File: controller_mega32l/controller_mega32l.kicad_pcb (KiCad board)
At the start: 2 copper layers, 262.9 x 144.8 mm, 81 parts, among them IC1 ATMEGA32-A, IC2 MAX481CPA, J1 RJ45, K1 CONN_PWR_OUT, P1 CONN_PWR_IN, P2 CONN_PWM_OUT, P3 CONN_3X2, P4 CONN_JTAG, P5 CONN_ADC, P6 CONN_GPIO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

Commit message: PCB signal layer
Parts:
- IC1: footprint TQFP44 -> Package_QFP:TQFP-44_10x10mm_P0.8mm
- IC2, J1, K1, P2, P3, P4, P5, P6, Q1, R14, R4: moved to F.Cu
- R17, R19, R20, R23, R25, R29, R30, R32: footprint C1 -> Resistor_THT:R_Axial_DIN0309_L9.0mm_D3.2mm_P15.24mm_Horizontal
- R27: moved to B.Cu
- R3: footprint C1 -> Resistor_THT:R_Axial_DIN0309_L9.0mm_D3.2mm_P20.32mm_Horizontal; moved to F.Cu
- moved R28 83.4 mm to (140.7, 83.8), turned to 270 degrees
- moved R18 52.9 mm to (118.6, 112.0)
- moved R3 26.5 mm to (182.6, 73.7), turned to 270 degrees
- moved R32 24.9 mm to (186.9, 103.4), turned to 180 degrees
- moved R27 20.8 mm to (83.8, 99.6)
- moved R29 20.1 mm to (187.5, 140.5)
- moved K1 19.4 mm to (107.4, 68.6), turned to 270 degrees
- moved P2 16.9 mm to (126.0, 69.6)
- moved R30 16.5 mm to (178.8, 140.5)
- moved D25 16.5 mm to (140.0, 123.2)
- moved R23 13.3 mm to (169.7, 140.2)
- moved R25 12.7 mm to (151.9, 139.7)
- moved R14 12.1 mm to (108.0, 86.4)
- moved P4 12.1 mm to (171.2, 73.4), turned to 270 degrees
- moved D14 10.2 mm to (156.4, 102.5)
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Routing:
- net (no net): track 156.0 -> 0.00 mm, vias 5 -> 0
- net DGND: track 0.00 -> 94.1 mm, vias 0 -> 3
- net +5VD: track 0.00 -> 77.9 mm
- net Net-(D14-Pad3): track 0.00 -> 49.6 mm, vias 0 -> 4
- net Net-(C2-Pad1): track 0.00 -> 43.1 mm
- net /TMS: track 0.00 -> 42.0 mm
- net /TDI: track 0.00 -> 37.5 mm
- net Net-(C4-Pad1): track 0.00 -> 36.4 mm
- net Net-(IC1-Pad12): track 0.00 -> 33.9 mm
- net Net-(IC1-Pad13): track 0.00 -> 27.6 mm
- net Net-(D8-Pad2): track 0.00 -> 20.5 mm
- net Net-(D10-Pad2): track 0.00 -> 20.1 mm
- net Net-(IC1-Pad26): track 0.00 -> 19.6 mm
- net /TDO: track 0.00 -> 19.5 mm
- net Net-(D11-Pad2): track 0.00 -> 15.9 mm
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- added copper zone on B.Cu, net +5VD
- removed copper zone on F.Cu, net +5VD
- removed copper zone on B.Cu, net DGND
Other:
- net class Default: clearance 0.35 -> 0.25; via_dia 1.27 -> 2.54
- rule trace_clearance: 0.35 -> 0.25

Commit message: PCB changes
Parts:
- removed D29: D_Schottky_x2_KCom_AAK, TO_SOT_Packages_SMD:SOT-23_Handsoldering
- D12: footprint TO_SOT_Packages_SMD:SOT-23_Handsoldering -> digikey-footprints:SOT-23-3
- P1: moved to F.Cu
- R1, R13, R27, R34: footprint C1 -> Resistor_THT:R_Axial_DIN0411_L9.9mm_D3.6mm_P15.24mm_Horizontal; moved to F.Cu
- R17, R19, R20, R23, R25, R29, R30, R32: footprint Resistor_THT:R_Axial_DIN0309_L9.0mm_D3.2mm_P15.24mm_Horizontal -> Resistor_THT:R_Axial_DIN0411_L9.9mm_D3.6mm_P15.24mm_Horizontal; moved to F.Cu
- R26, R4: footprint C1 -> Resistor_THT:R_Axial_DIN0411_L9.9mm_D3.6mm_P15.24mm_Horizontal
- R3: footprint Resistor_THT:R_Axial_DIN0309_L9.0mm_D3.2mm_P20.32mm_Horizontal -> Resistor_THT:R_Axial_DIN0411_L9.9mm_D3.6mm_P20.32mm_Horizontal
- moved R26 18.1 mm to (76.7, 93.7)
- moved R25 17.8 mm to (169.7, 140.2)
- moved R1 16.9 mm to (61.0, 53.6)
- moved R4 15.5 mm to (178.1, 97.5)
- moved R13 13.7 mm to (87.4, 108.2)
- moved R20 9.40 mm to (151.4, 140.0)
- moved R23 9.40 mm to (160.3, 140.5)
- moved R19 6.37 mm to (142.7, 145.3)
- moved P1 6.10 mm to (45.7, 63.8)
- moved R17 5.73 mm to (135.9, 145.3)
- moved R27 4.79 mm to (86.4, 103.6)
- moved R34 4.75 mm to (48.5, 89.2)
- moved D18 3.23 mm to (65.5, 98.8)
- moved K1 0.80 mm to (107.7, 69.3)
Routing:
- net DGND: track 94.1 -> 84.7 mm

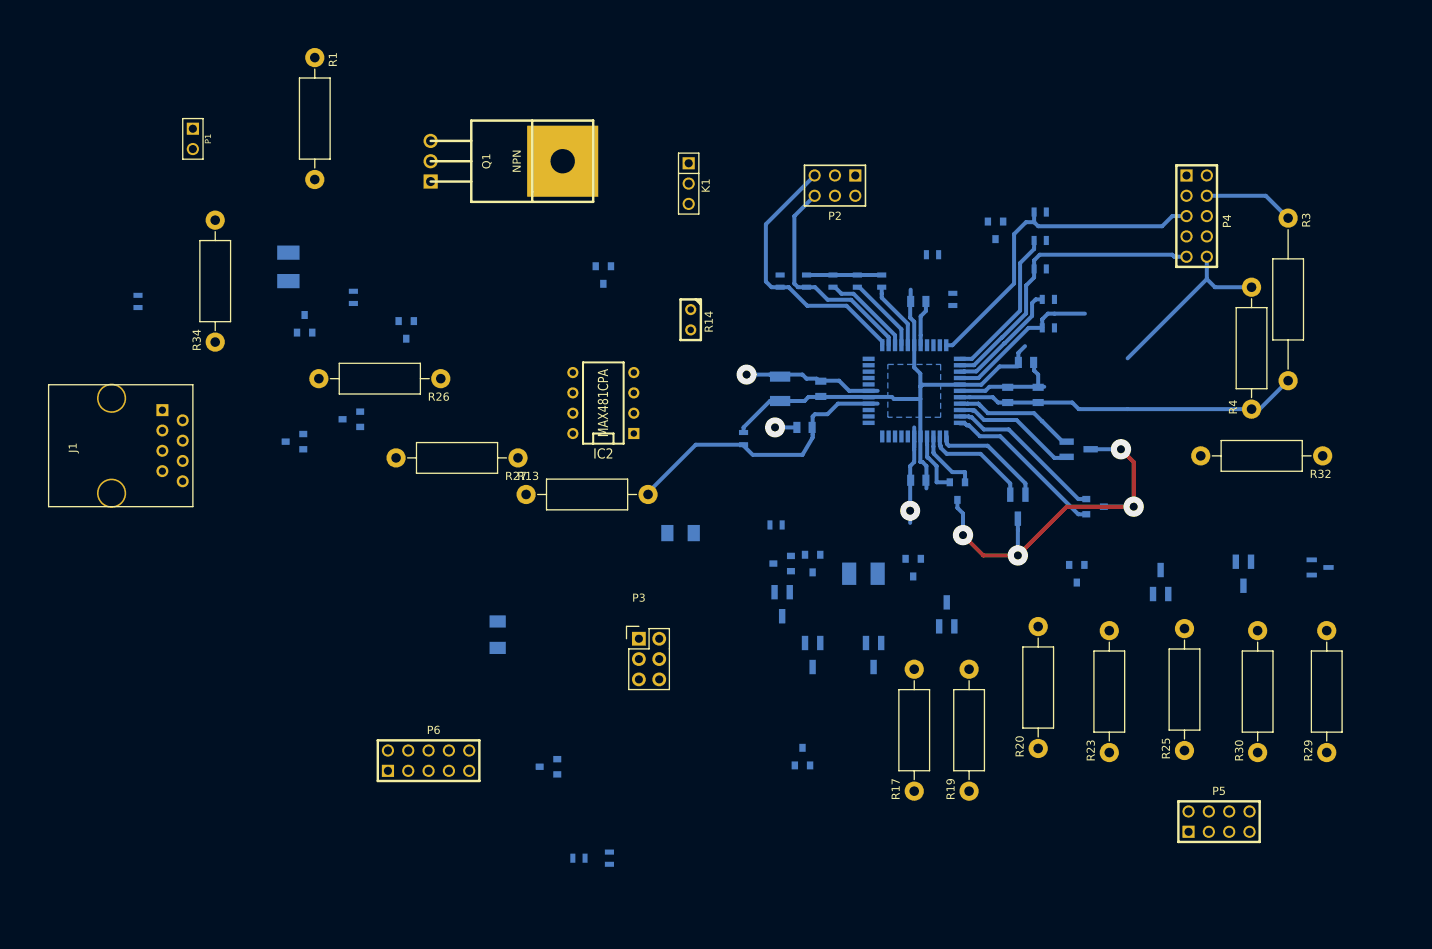
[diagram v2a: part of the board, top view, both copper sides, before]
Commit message: New PCB routes, footprints updated, KiCAD up version to 5.1
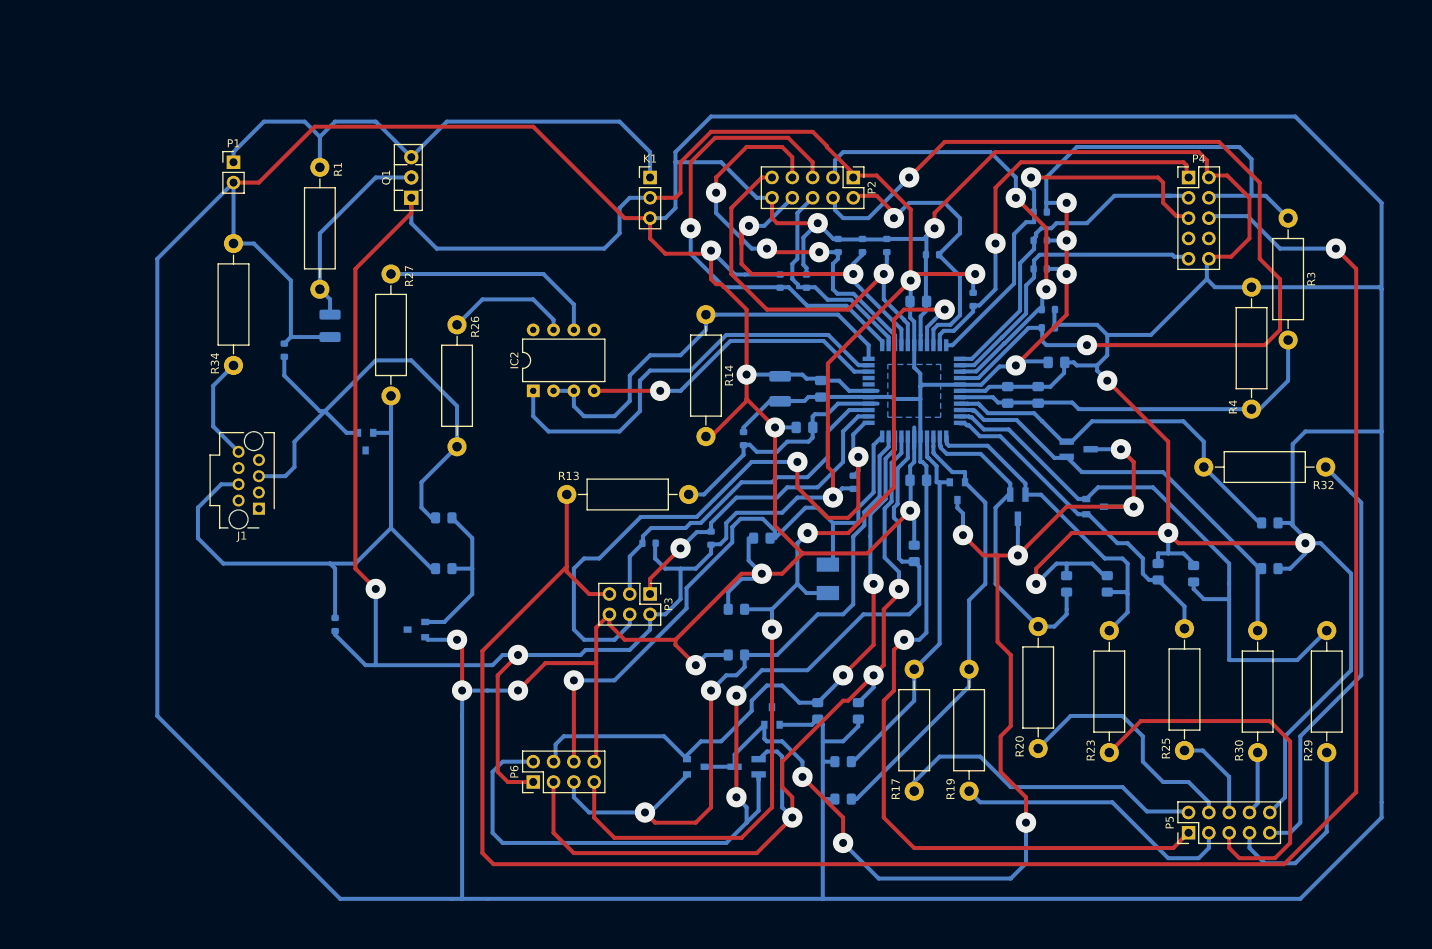
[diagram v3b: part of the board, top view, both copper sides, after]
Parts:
- C1: footprint SM1210 -> Capacitor_SMD:C_1210_3225Metric_Pad1.33x2.70mm_HandSolder
- C2, C3, C4, C5, C6, C7, C8: footprint SM0805 -> Capacitor_SMD:C_0805_2012Metric_Pad1.18x1.45mm_HandSolder
- D1: footprint SM1210L -> Diode_SMD:D_1210_3225Metric
- D10, D2, D25, D4, D8: footprint TO_SOT_Packages_SMD:SOT-23_Handsoldering -> Diode_SMD:D_0805_2012Metric_Pad1.15x1.40mm_HandSolder
- D11, D13, D18, D23, D26, D28, D5, D7: footprint SOT23 -> Diode_SMD:D_0805_2012Metric_Pad1.15x1.40mm_HandSolder
- D12: footprint digikey-footprints:SOT-23-3 -> Diode_SMD:D_0805_2012Metric_Pad1.15x1.40mm_HandSolder
- D21, D22: footprint SM1206 -> Diode_SMD:D_0805_2012Metric_Pad1.15x1.40mm_HandSolder
- IC2: footprint DIP-8__300 -> Package_DIP:DIP-8_W7.62mm
- J1: footprint RJ45_8 -> Connector_RJ:RJ45_Plug_Metz_AJP92A8813
- K1: footprint PIN_ARRAY_3X1 -> Connector_PinHeader_2.54mm:PinHeader_1x03_P2.54mm_Vertical
- P1: footprint PIN_ARRAY_2X1 -> Connector_PinHeader_2.54mm:PinHeader_1x02_P2.54mm_Vertical
- P2: footprint pin_array_3x2 -> Connector_PinHeader_2.54mm:PinHeader_2x05_P2.54mm_Vertical
- P3: footprint Pin_Headers:Pin_Header_Straight_2x03 -> Connector_PinHeader_2.54mm:PinHeader_2x03_P2.54mm_Vertical
- P4: footprint PIN_ARRAY_5x2 -> Connector_PinHeader_2.54mm:PinHeader_2x05_P2.54mm_Vertical
- P5: footprint pin_array_4x2 -> Connector_PinHeader_2.54mm:PinHeader_2x05_P2.54mm_Vertical
- P6: footprint PIN_ARRAY_5x2 -> Connector_PinHeader_2.54mm:PinHeader_2x04_P2.54mm_Vertical
- Q1: footprint TO220 -> Package_TO_SOT_THT:TO-126-3_Vertical
- R10, R11, R12, R15, R16, R18, R2, R21, R22, R24, R28, R31, R33, R5, R6, R7, R8, R9: footprint SM0603 -> Resistor_SMD:R_0603_1608Metric
- R14: footprint C1 -> Resistor_THT:R_Axial_DIN0411_L9.9mm_D3.6mm_P15.24mm_Horizontal
- R3: footprint Resistor_THT:R_Axial_DIN0411_L9.9mm_D3.6mm_P20.32mm_Horizontal -> Resistor_THT:R_Axial_DIN0411_L9.9mm_D3.6mm_P15.24mm_Horizontal
- moved D26 62.5 mm to (128.9, 135.3), turned to 90 degrees
- moved D23 50.3 mm to (113.7, 128.3)
- moved R31 47.3 mm to (63.5, 124.5), turned to 90 degrees
- moved R16 43.3 mm to (110.5, 113.7), turned to 90 degrees
- moved D7 40.7 mm to (160.0, 119.4)
- moved R15 39.7 mm to (102.7, 114.3), turned to 180 degrees
- moved D17 37.5 mm to (73.7, 125.1), turned to 270 degrees
- moved D5 31.9 mm to (154.9, 119.4), turned to 270 degrees
- moved D21 30.0 mm to (113.7, 122.6), turned to 0 degrees
- moved D13 29.8 mm to (77.1, 111.1)
- moved R27 27.9 mm to (70.5, 80.6), turned to 270 degrees
- moved D11 24.1 mm to (180.3, 117.5), turned to 180 degrees
- moved D18 22.0 mm to (77.1, 117.5), turned to 180 degrees
- moved D27 20.8 mm to (114.9, 142.2), turned to 270 degrees
- moved D25 20.1 mm to (123.8, 135.3), turned to 90 degrees
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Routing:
- net DGND: track 84.7 -> 1144.8 mm, vias 3 -> 15
- net +5VD: track 77.9 -> 535.7 mm, vias 0 -> 10
- net /-RESET: track 0.00 -> 256.7 mm, vias 0 -> 1
- net /GPIO_1: track 0.00 -> 121.8 mm, vias 0 -> 2
- net /GPIO_6: track 0.00 -> 119.5 mm, vias 0 -> 3
- net /GPIO_2: track 0.00 -> 112.1 mm, vias 0 -> 3
- net Net-(IC1-Pad26): track 19.6 -> 126.1 mm, vias 0 -> 2
- net Net-(D14-Pad3): track 49.6 -> 146.6 mm, vias 4 -> 7
- net /GPIO_4: track 0.00 -> 89.0 mm, vias 0 -> 2
- net /GPIO_3: track 0.00 -> 79.9 mm, vias 0 -> 2
- net /GPIO_5: track 0.00 -> 78.2 mm, vias 0 -> 1
- net Net-(IC1-Pad1): track 0.00 -> 78.2 mm, vias 0 -> 2
- net Net-(D15-Pad2): track 0.00 -> 70.9 mm
- net +24V: track 0.00 -> 68.7 mm
- net Net-(D13-Pad2): track 0.00 -> 66.3 mm
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
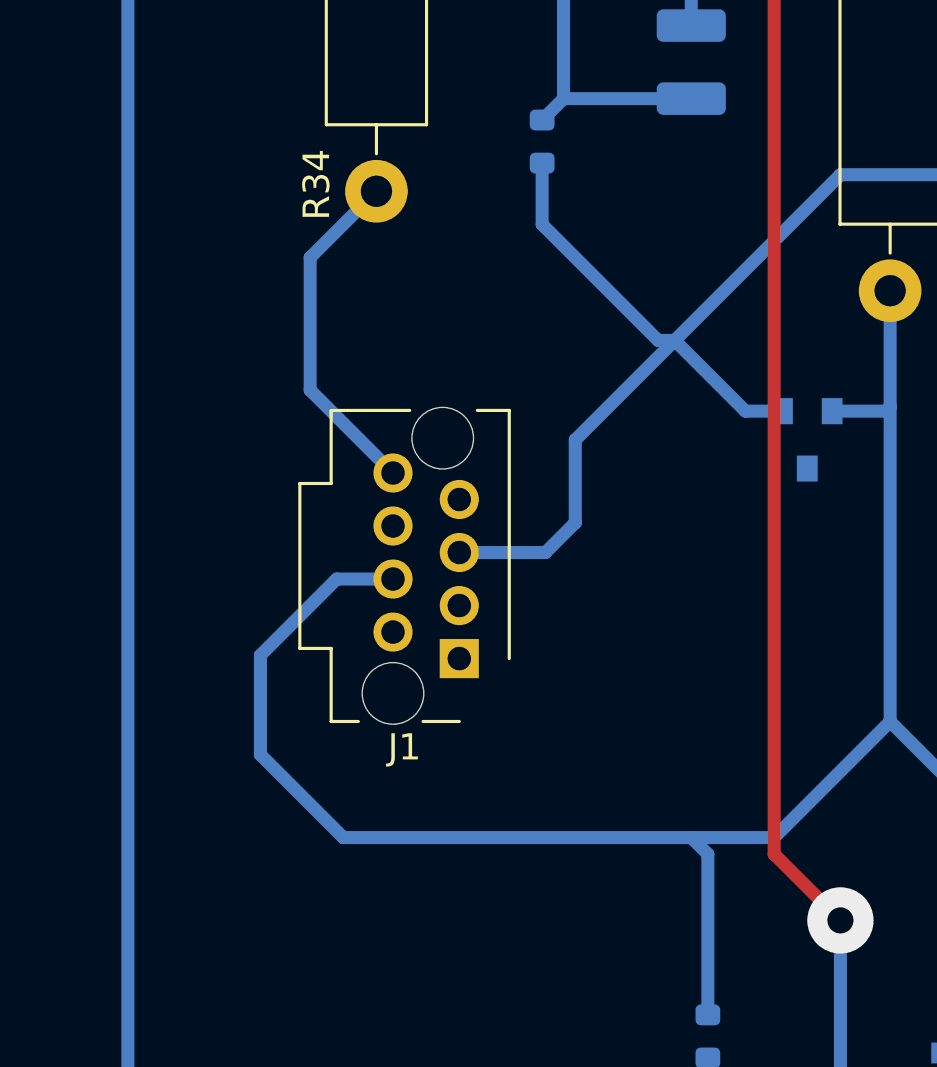
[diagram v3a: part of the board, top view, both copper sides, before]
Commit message: RJ-45 footprint updated, PCB screenshot added to docs
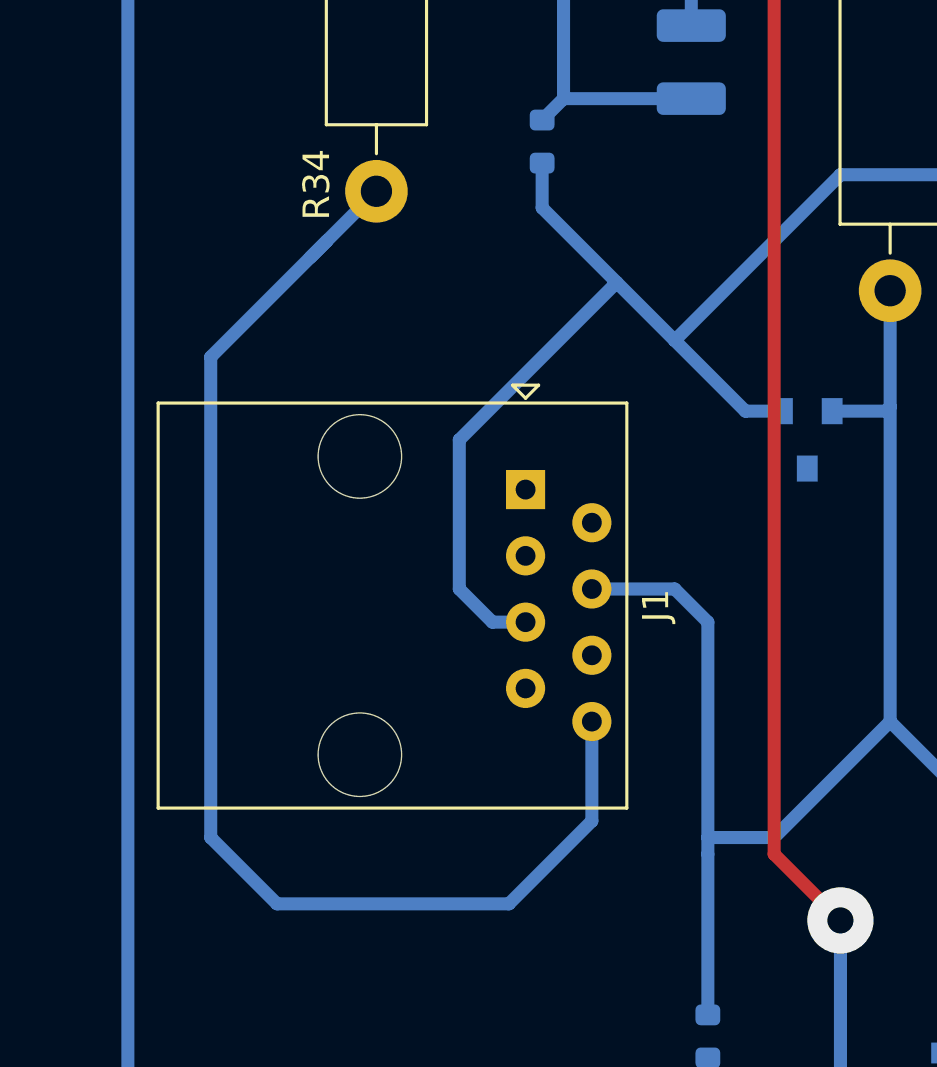
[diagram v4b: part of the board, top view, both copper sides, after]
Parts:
- J1: footprint Connector_RJ:RJ45_Plug_Metz_AJP92A8813 -> Connector_RJ:RJ45_Amphenol_54602-x08_Horizontal
- moved J1 6.96 mm to (56.5, 103.5), turned to 270 degrees
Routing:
- net Net-(J1-Pad8): track 13.2 -> 49.1 mm
- net Net-(D15-Pad2): track 70.9 -> 55.3 mm
- net Net-(D13-Pad2): track 66.3 -> 69.8 mm

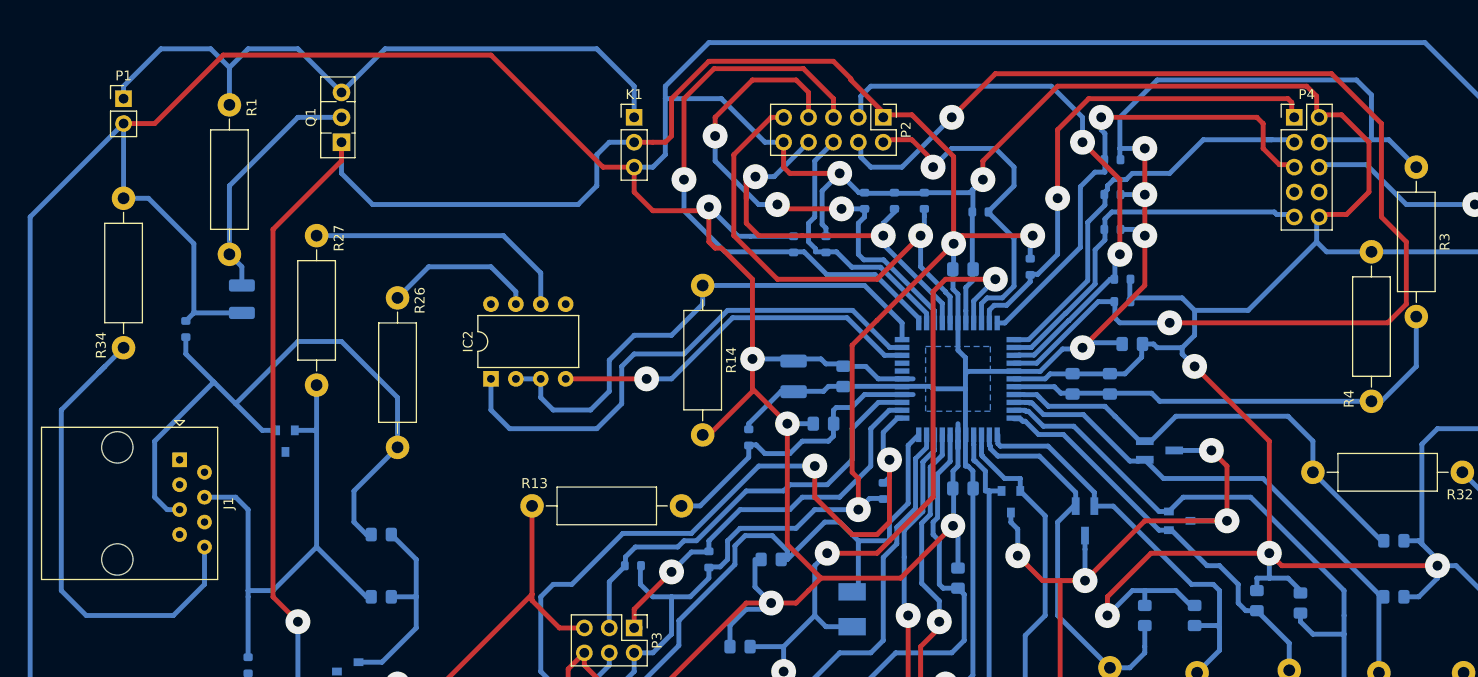
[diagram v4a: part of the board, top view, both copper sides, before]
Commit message: RJ-45 ground connections fixed, PCB texts placed right
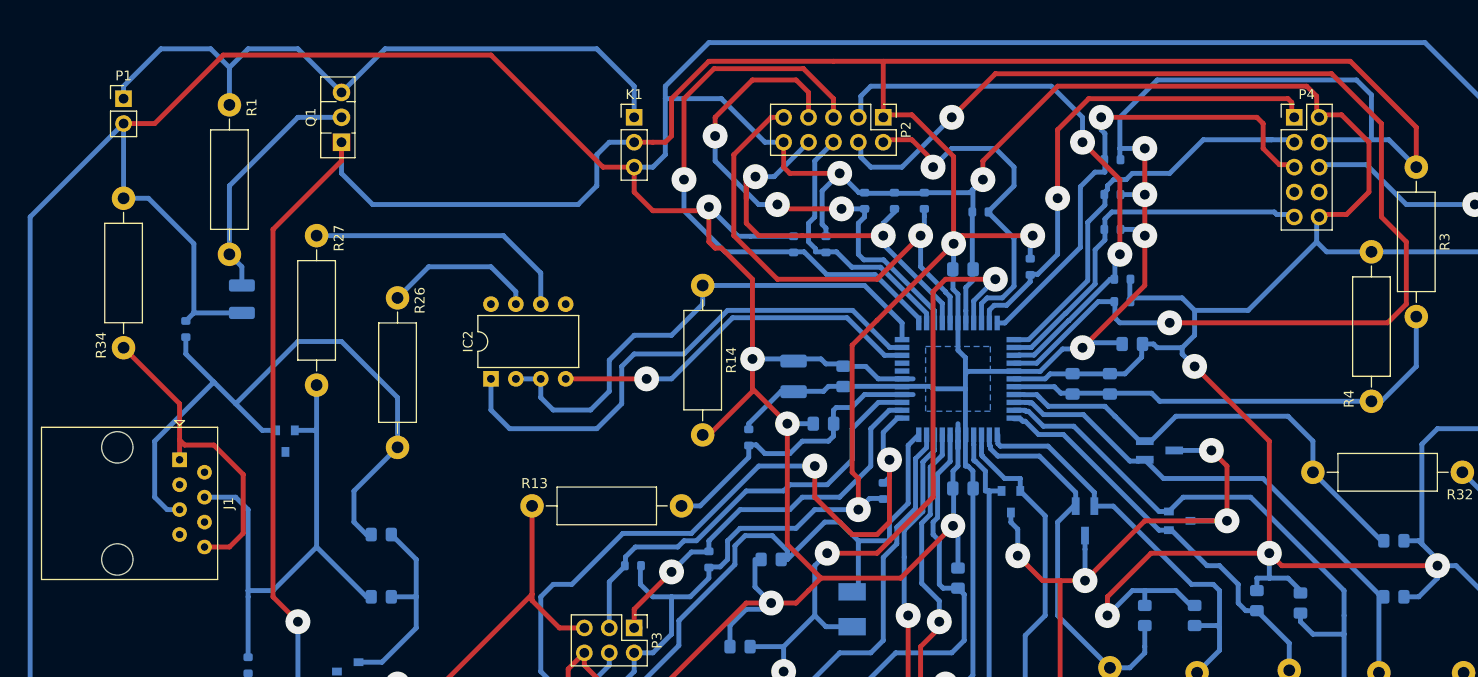
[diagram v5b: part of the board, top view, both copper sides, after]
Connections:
- J1 pad 8: Net-(J1-Pad8) -> Net-(J1-Pad1)
- R34 pad 1: Net-(J1-Pad8) -> Net-(J1-Pad1)
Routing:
- net +5VD: track 535.7 -> 600.1 mm
- net Net-(J1-Pad8): track 49.1 -> 0.00 mm
- net Net-(J1-Pad1): track 0.00 -> 32.3 mm
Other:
- rule via_min_size: 0.889 -> 1

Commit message: PCB board outer dimensions added
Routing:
- net DGND: track 1144.8 -> 1137.0 mm
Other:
- board size 262.9 x 144.8 mm -> 156 x 100 mm
